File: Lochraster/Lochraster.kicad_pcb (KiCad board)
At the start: 2 copper layers, 54.6 x 53.3 mm, 25 parts, among them J1 Conn_01x04_Pin, J2 Conn_01x32_Pin, J3 Conn_01x04_Pin, J4 Conn_01x07_Pin, J5 Conn_01x08_Pin, J6 Conn_01x04_Pin, J7 Conn_01x08_Pin, J8 Conn_01x04_Pin, J9 Conn_01x04_Pin

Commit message: final version V1.0
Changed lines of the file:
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@@
     (property "ki_description" "Generic connector, single row, 01x04, script generated")
     (property "ki_keywords" "connector")
-    (attr through_hole)
+    (attr through_hole exclude_from_pos_files)
     (fp_text reference "J6" (at 0 -2.77 90) (layer "F.SilkS") hide
         (effects (font (size 1 1) (thickness 0.15)))
@@
     (property "ki_description" "Generic connector, single row, 01x08, script generated")
     (property "ki_keywords" "connector")
-    (attr through_hole)
+    (attr through_hole exclude_from_pos_files)
     (fp_text reference "J7" (at 0 -2.77 90) (layer "F.SilkS") hide
         (effects (font (size 1 1) (thickness 0.15)))
@@
     (property "ki_description" "Generic connector, single row, 01x32, script generated")
     (property "ki_keywords" "connector")
-    (attr through_hole)
+    (attr through_hole exclude_from_pos_files)
     (fp_text reference "J2" (at -1.27 -2.77 180) (layer "F.SilkS") hide
         (effects (font (size 1 1) (thickness 0.15)))
@@
     (property "ki_description" "Generic connector, single row, 01x04, script generated")
     (property "ki_keywords" "connector")
-    (attr through_hole)
+    (attr through_hole exclude_from_pos_files)
     (fp_text reference "J8" (at 0 -2.33) (layer "F.SilkS") hide
         (effects (font (size 1 1) (thickness 0.15)))
@@
     (property "ki_description" "Generic connector, single row, 01x08, script generated")
     (property "ki_keywords" "connector")
-    (attr through_hole)
+    (attr through_hole exclude_from_pos_files)
     (fp_text reference "J5" (at 0 -2.77 90) (layer "F.SilkS") hide
         (effects (font (size 1 1) (thickness 0.15)))
@@
     (property "ki_description" "Generic connector, single row, 01x07, script generated")
     (property "ki_keywords" "connector")
-    (attr through_hole)
+    (attr through_hole exclude_from_pos_files)
     (fp_text reference "J4" (at 0 -2.77 90) (layer "F.SilkS") hide
         (effects (font (size 1 1) (thickness 0.15)))
@@
     (property "ki_description" "Generic connector, single row, 01x04, script generated")
     (property "ki_keywords" "connector")
-    (attr through_hole)
+    (attr through_hole exclude_from_pos_files)
     (fp_text reference "J9" (at 0 -2.33) (layer "F.SilkS") hide
         (effects (font (size 1 1) (thickness 0.15)))
@@
     (property "ki_description" "Generic connector, single row, 01x04, script generated")
     (property "ki_keywords" "connector")
-    (attr through_hole)
+    (attr through_hole exclude_from_pos_files)
     (fp_text reference "J1" (at 0 -2.33) (layer "F.SilkS") hide
         (effects (font (size 1 1) (thickness 0.15)))
@@
     (property "ki_description" "Generic connector, single row, 01x04, script generated")
     (property "ki_keywords" "connector")
-    (attr through_hole)
+    (attr through_hole exclude_from_pos_files)
     (fp_text reference "J3" (at 0 -2.33) (layer "F.SilkS") hide
         (effects (font (size 1 1) (thickness 0.15)))
@@
         (effects (font (size 1 1) (thickness 0.15)) (justify mirror))
     )
-    (fp_line (start 0 -53.34) (end 0 0)
-      (stroke (width 0.15) (type solid)) (layer "B.SilkS"))
-    (fp_line (start 0 -53.34) (end 97.536 -53.34)
-      (stroke (width 0.15) (type solid)) (layer "B.SilkS"))
-    (fp_line (start 0 0) (end 99.06 0)
-      (stroke (width 0.15) (type solid)) (layer "B.SilkS"))
-    (fp_line (start 97.536 -53.34) (end 99.06 -51.816)
-      (stroke (width 0.15) (type solid)) (layer "B.SilkS"))
-    (fp_line (start 99.06 -40.64) (end 99.06 -51.816)
-      (stroke (width 0.15) (type solid)) (layer "B.SilkS"))
-    (fp_line (start 99.06 -1.27) (end 101.6 -3.81)
-      (stroke (width 0.15) (type solid)) (layer "B.SilkS"))
-    (fp_line (start 99.06 0) (end 99.06 -1.27)
-      (stroke (width 0.15) (type solid)) (layer "B.SilkS"))
-    (fp_line (start 101.6 -38.1) (end 99.06 -40.64)
-      (stroke (width 0.15) (type solid)) (layer "B.SilkS"))
-    (fp_line (start 101.6 -3.81) (end 101.6 -38.1)
-      (stroke (width 0.15) (type solid)) (layer "B.SilkS"))
-    (fp_circle (center 13.97 -2.54) (end 17.42 -2.54)
-      (stroke (width 0.15) (type solid)) (fill none) (layer "F.CrtYd"))
-    (fp_circle (center 15.24 -50.8) (end 18.69 -50.8)
-      (stroke (width 0.15) (type solid)) (fill none) (layer "F.CrtYd"))
     (fp_circle (center 90.17 -50.8) (end 93.62 -50.8)
       (stroke (width 0.15) (type solid)) (fill none) (layer "F.CrtYd"))
     (fp_circle (center 96.52 -2.54) (end 99.97 -2.54)
       (stroke (width 0.15) (type solid)) (fill none) (layer "F.CrtYd"))
-    (fp_line (start -6.34 -44.0036) (end 9.41 -44.0036)
-      (stroke (width 0.15) (type solid)) (layer "B.Fab"))
-    (fp_line (start -6.34 -32.1936) (end -6.34 -44.0036)
-      (stroke (width 0.15) (type solid)) (layer "B.Fab"))
-    (fp_line (start -6.34 -32.1936) (end 9.41 -32.1936)
-      (stroke (width 0.15) (type solid)) (layer "B.Fab"))
-    (fp_line (start -1.68 -12.2936) (end -1.68 -3.3026)
-      (stroke (width 0.15) (type solid)) (layer "B.Fab"))
-    (fp_line (start -1.68 -12.2936) (end 11.81 -12.2936)
-      (stroke (width 0.15) (type solid)) (layer "B.Fab"))
-    (fp_line (start -1.68 -3.3026) (end 11.81 -3.3026)
-      (stroke (width 0.15) (type solid)) (layer "B.Fab"))
-    (fp_line (start 9.41 -32.1936) (end 9.41 -44.0036)
-      (stroke (width 0.15) (type solid)) (layer "B.Fab"))
-    (fp_line (start 11.81 -12.2936) (end 11.81 -3.3026)
-      (stroke (width 0.15) (type solid)) (layer "B.Fab"))
-    (fp_rect (start 17.526 -52.07) (end 42.926 -49.53)
-      (stroke (width 0.1) (type solid)) (fill none) (layer "B.Fab"))
-    (fp_rect (start 26.67 -3.81) (end 46.99 -1.27)
-      (stroke (width 0.1) (type solid)) (fill none) (layer "B.Fab"))
     (fp_rect (start 44.45 -52.07) (end 64.77 -49.53)
       (stroke (width 0.1) (type solid)) (fill none) (layer "B.Fab"))
@@
     (fp_rect (start 92.71 -52.07) (end 97.79 -6.35)
       (stroke (width 0.1) (type solid)) (fill none) (layer "B.Fab"))
-    (fp_circle (center 13.97 -2.54) (end 17.17 -2.54)
-      (stroke (width 0.15) (type solid)) (fill none) (layer "B.Fab"))
-    (fp_circle (center 15.24 -50.8) (end 18.44 -50.8)
-      (stroke (width 0.15) (type solid)) (fill none) (layer "B.Fab"))
     (fp_circle (center 90.17 -50.8) (end 93.37 -50.8)
       (stroke (width 0.15) (type solid)) (fill none) (layer "B.Fab"))
     (fp_circle (center 96.52 -2.54) (end 99.72 -2.54)
       (stroke (width 0.15) (type solid)) (fill none) (layer "B.Fab"))
-    (fp_circle (center 13.97 -2.54) (end 17.17 -2.54)
-      (stroke (width 0.15) (type solid)) (fill none) (layer "F.Fab"))
-    (fp_circle (center 15.24 -50.8) (end 18.44 -50.8)
-      (stroke (width 0.15) (type solid)) (fill none) (layer "F.Fab"))
     (fp_circle (center 90.17 -50.8) (end 93.37 -50.8)
       (stroke (width 0.15) (type solid)) (fill none) (layer "F.Fab"))
     (fp_circle (center 96.52 -2.54) (end 99.72 -2.54)
       (stroke (width 0.15) (type solid)) (fill none) (layer "F.Fab"))
-    (pad "" np_thru_hole circle locked (at 13.97 -2.54) (size 3.2 3.2) (drill 3.2) (layers "*.Cu" "*.Mask"))
     (pad "" np_thru_hole circle locked (at 90.17 -50.8) (size 3.2 3.2) (drill 3.2) (layers "*.Cu" "*.Mask"))
     (pad "" np_thru_hole circle locked (at 96.52 -2.54) (size 3.2 3.2) (drill 3.2) (layers "*.Cu" "*.Mask"))
@@
     (effects (font (size 0.5 0.5) (thickness 0.1) bold) (justify left bottom))
   )
+  (dimension (type aligned) (layer "F.Fab")
+    (pts (xy 211.013 105.26) (xy 211.013 51.92))
+    (height 11.43)
+    (gr_text "53,3400 mm" (at 221.293 78.59 90) (layer "F.Fab")
+      (effects (font (size 1 1) (thickness 0.15)))
+    )
+    (format (prefix "") (suffix "") (units 3) (units_format 1) (precision 4))
+    (style (thickness 0.1) (arrow_length 1.27) (text_position_mode 0) (extension_height 0.58642) (extension_offset 0.5) keep_text_aligned)
+  )
+  (dimension (type aligned) (layer "F.Fab")
+    (pts (xy 156.403 51.92) (xy 211.013 51.92))
+    (height -3.81)
+    (gr_text "54,6100 mm" (at 183.708 46.96) (layer "F.Fab")
+      (effects (font (size 1 1) (thickness 0.15)))
+    )
+    (format (prefix "") (suffix "") (units 3) (units_format 1) (precision 4))
+    (style (thickness 0.1) (arrow_length 1.27) (text_position_mode 0) (extension_height 0.58642) (extension_offset 0.5) keep_text_aligned)
+  )
   (segment (start 162.753 64.65) (end 160.243 64.65) (width 1) (layer "F.Cu") (net 1))

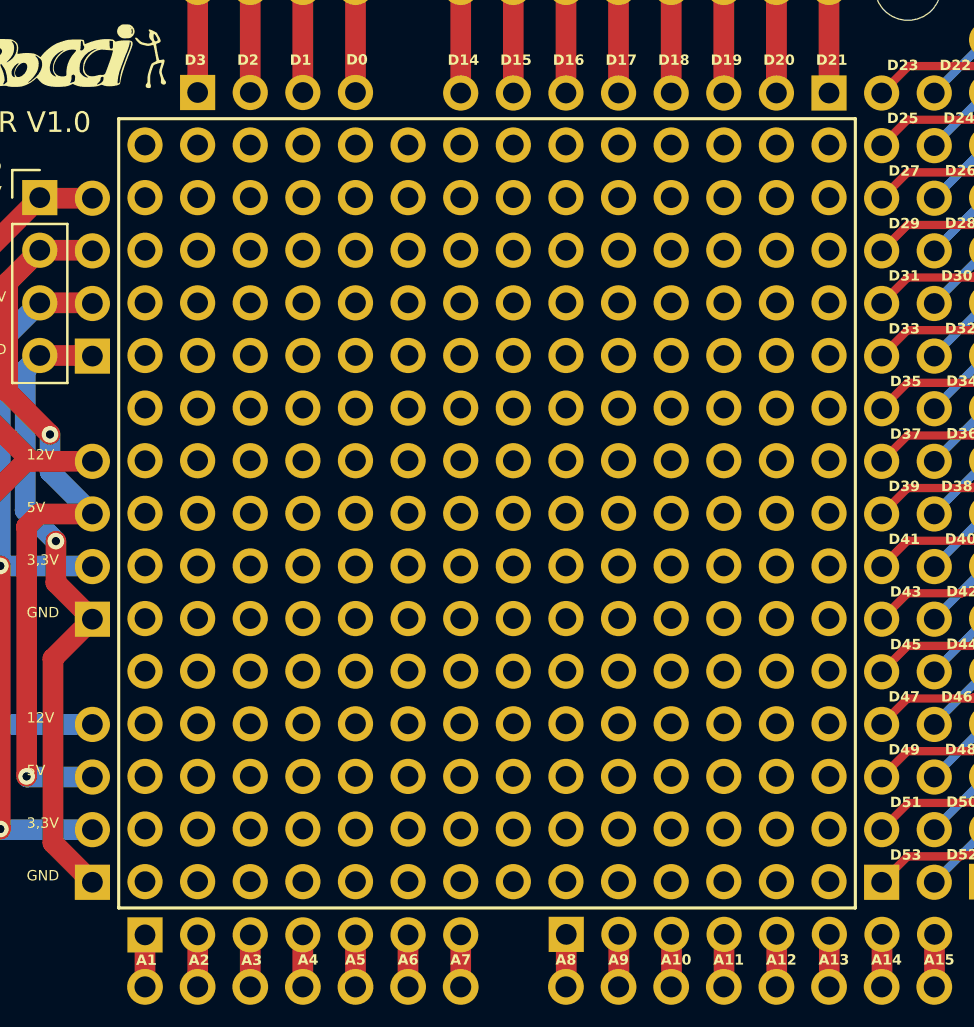
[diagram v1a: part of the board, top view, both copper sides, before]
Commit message: rework Lochraster for larger pads
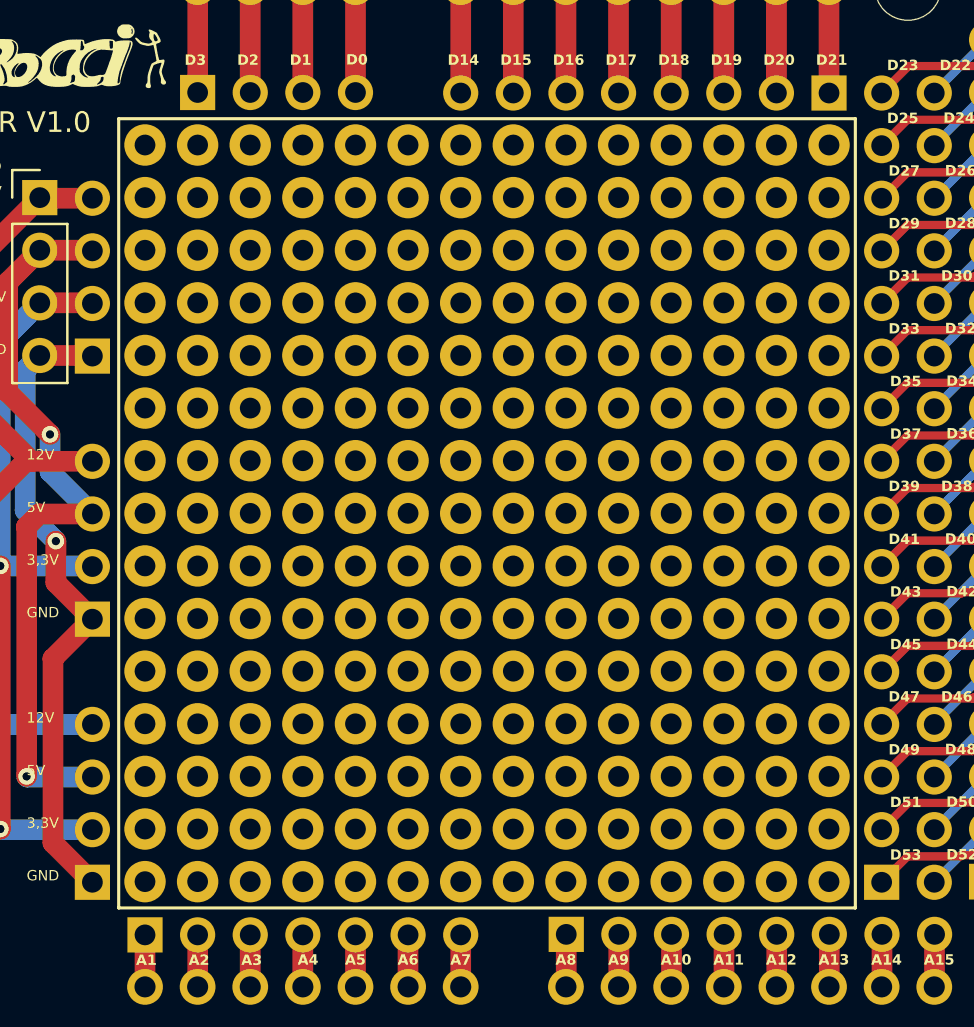
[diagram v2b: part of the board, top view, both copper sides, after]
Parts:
- REF** (x14): footprint Connector_PinSocket_2.54mm:PinSocket_1x15_P2.54mm_Vertical -> Library:lochraster
